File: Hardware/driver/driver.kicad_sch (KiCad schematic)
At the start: 0 parts

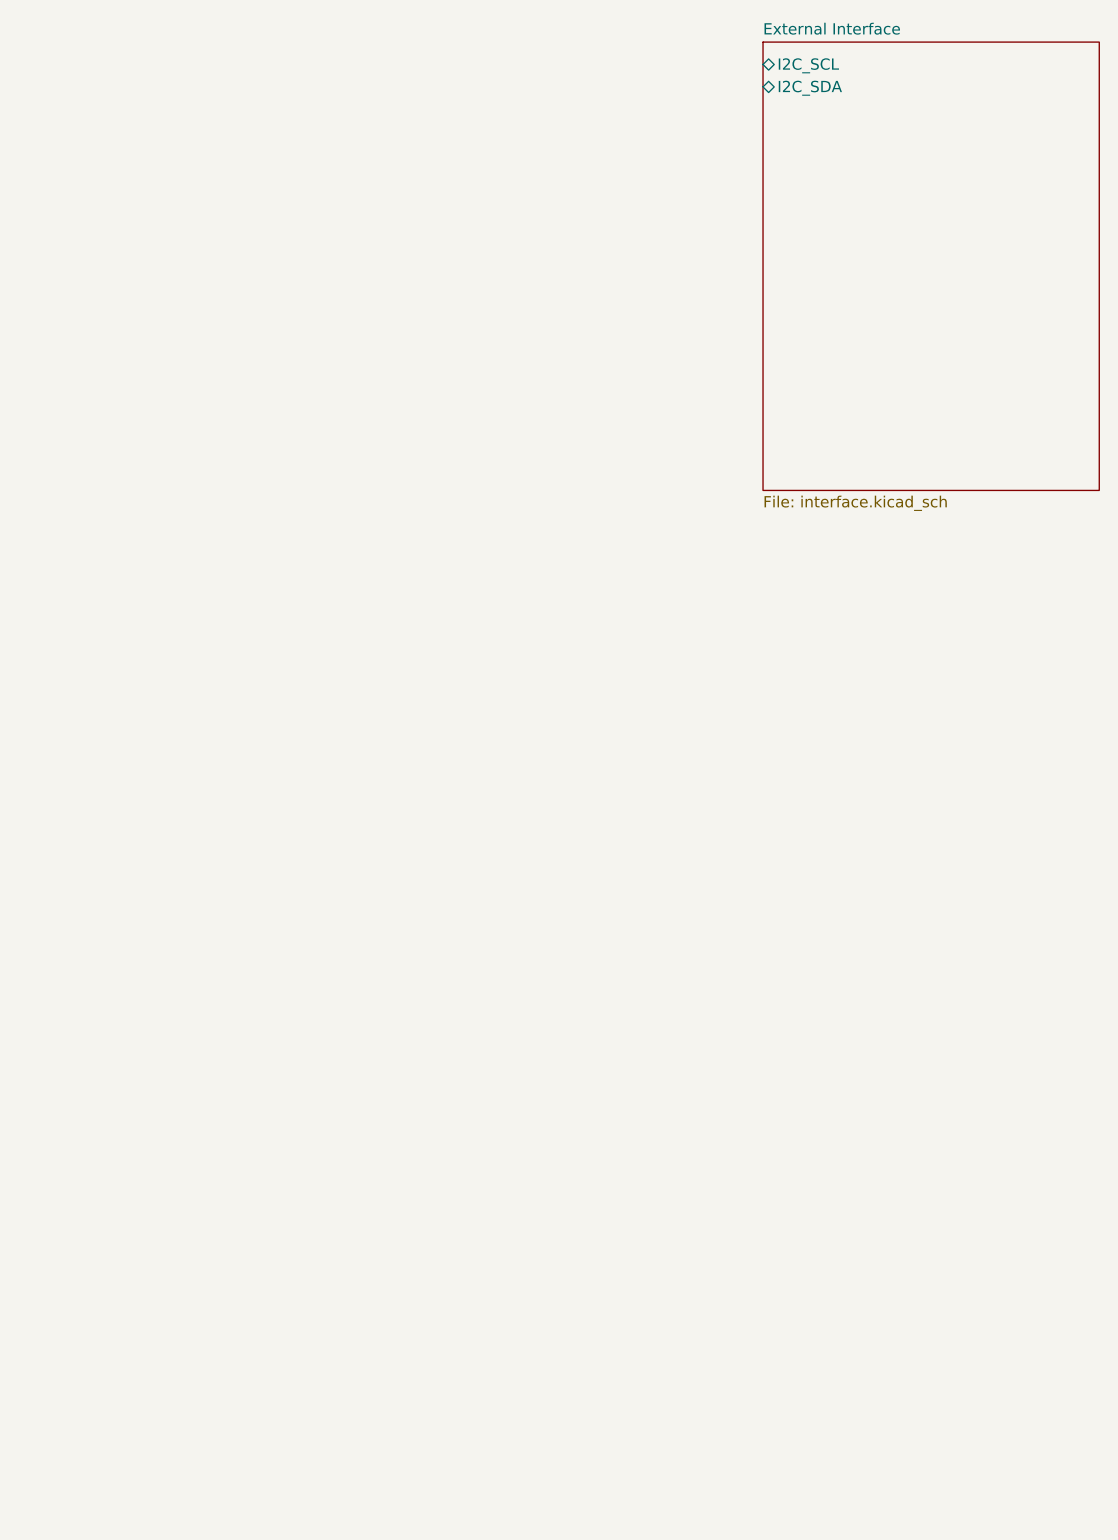
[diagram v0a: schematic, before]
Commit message: Placed all peripherals, start input
- Created footprints/symbols for some required I2C devices, including
  all DACs and ADCs, and placed them on the input section schematic

- Started work on heatsink footprint (C40-058-AE)

- Placed input connector for input. This is a pluggable screw terminal,
  which would then in turn connect to front panel jacks/banana plugs for
  external connectivity. This is good for roughly 20A, which is what the
  fuse (and our maximum rating for now) shall be
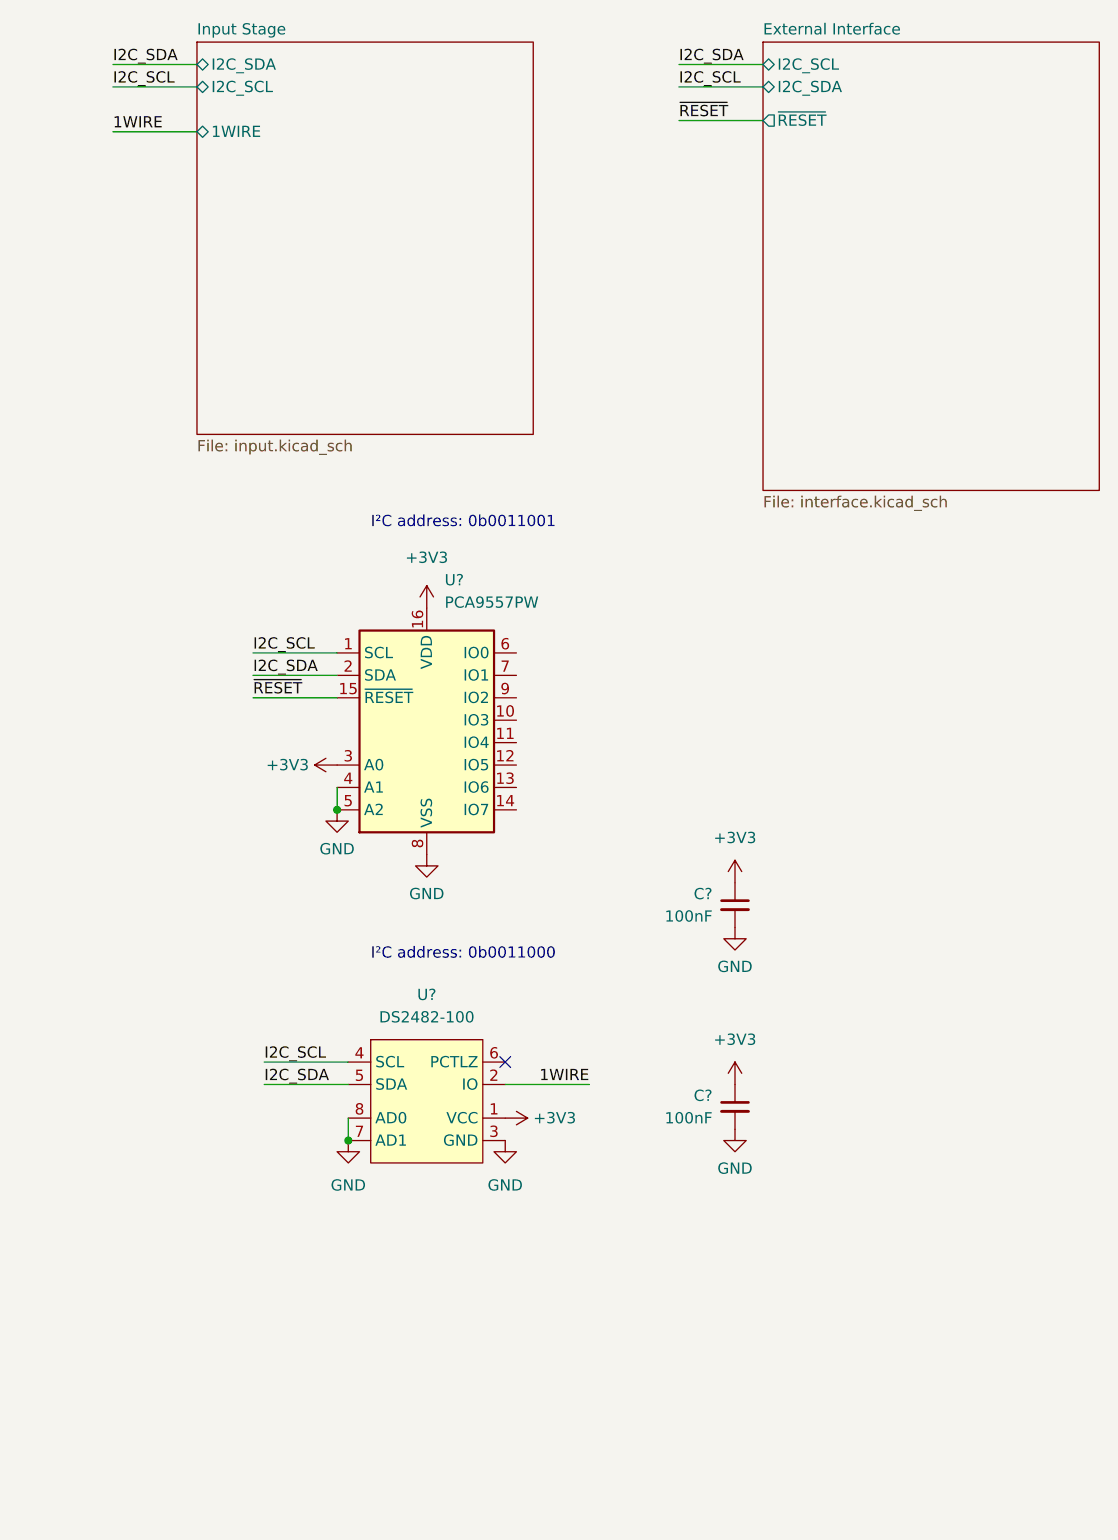
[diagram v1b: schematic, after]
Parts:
- added C? (x2): 100nF, Capacitor_SMD:C_0805_2012Metric_Pad1.18x1.45mm_HandSolder, symbol Device:C_Small
- added U?: DS2482-100, Package_SO:SO-8_3.9x4.9mm_P1.27mm, symbol programmable-load:DS2482-100
- added U?: PCA9557PW, Package_SO:TSSOP-16_4.4x5mm_P0.65mm, symbol Interface_Expansion:PCA9557PW
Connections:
- new net +3V3: C?.1, C?.1, U?.1 (VCC), U?.16 (VDD), U?.3 (A0)
- new net 1WIRE: U?.2 (IO)
- new net GND: C?.2, C?.2, U?.3 (GND), U?.4 (A1), U?.5 (A2), U?.7 (AD1), U?.8 (AD0), U?.8 (VSS)
- new net I2C_SCL: U?.1 (SCL), U?.4 (SCL)
- new net I2C_SDA: U?.2 (SDA), U?.5 (SDA)
- new net ~{RESET}: U?.15 (~{RESET})
- no-connect marks 0 -> 1
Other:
- added sheet Input Stage (input.kicad_sch)
- sheet External Interface ports: added ~{RESET}; removed none
- note added: "I²C address: 0b0011000"
- note added: "I²C address: 0b0011001"

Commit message: Basic board layout shape
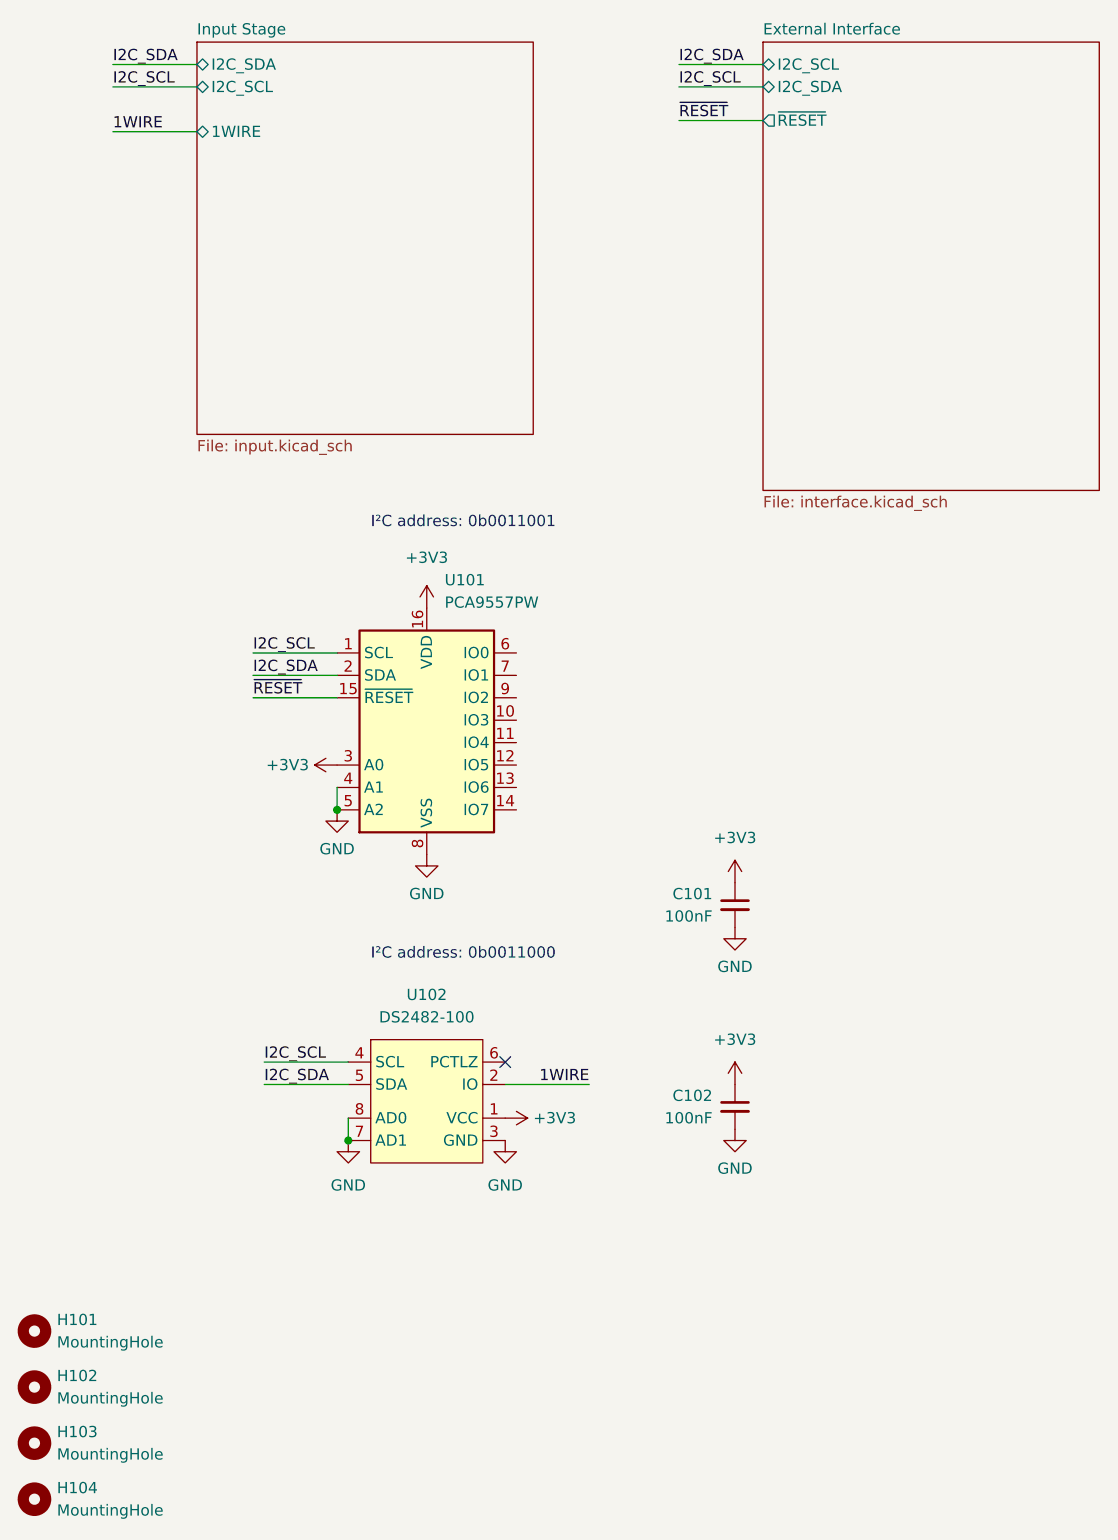
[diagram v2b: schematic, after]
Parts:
- added H101, H102, H103, H104: MountingHole, MountingHole:MountingHole_3.5mm, symbol Mechanical:MountingHole
- gave numbers to parts that had none: 4
